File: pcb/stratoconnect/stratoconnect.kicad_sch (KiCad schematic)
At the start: 38 parts, among them J1 Conn_Coaxial, J2 Conn_02x03_Odd_Even, J3 Conn_01x05_Male, J4 Conn_01x02_Male, J5 Conn_01x03_Male, SW1 SW_SPST, SW2 SW_SPST, U1 RF4463f30, U2 ATmega328PB-A, U3 TPS61022RWU, Y1 CSTNE16M0V530000R0

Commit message: WIP
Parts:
- added R10, R11: 22k, Resistor_SMD:R_0603_1608Metric, symbol Device:R_Small_US
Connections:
- net RX_LED is gone; now on net LED_RX: R7.1
- net TX_LED is gone; now on net LED_TX: R6.1
- net +5V: now also R10.1, R11.1
- net LED_RX: no longer U2.2 (PD4)
- net LED_TX: no longer U2.1 (PD3)
- net SCL: now also R10.2
- net SDA: now also R11.2
- net TRIG: now also U2.1 (PD3)
- no-connect marks 9 -> 13
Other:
- moved on the sheet: J3

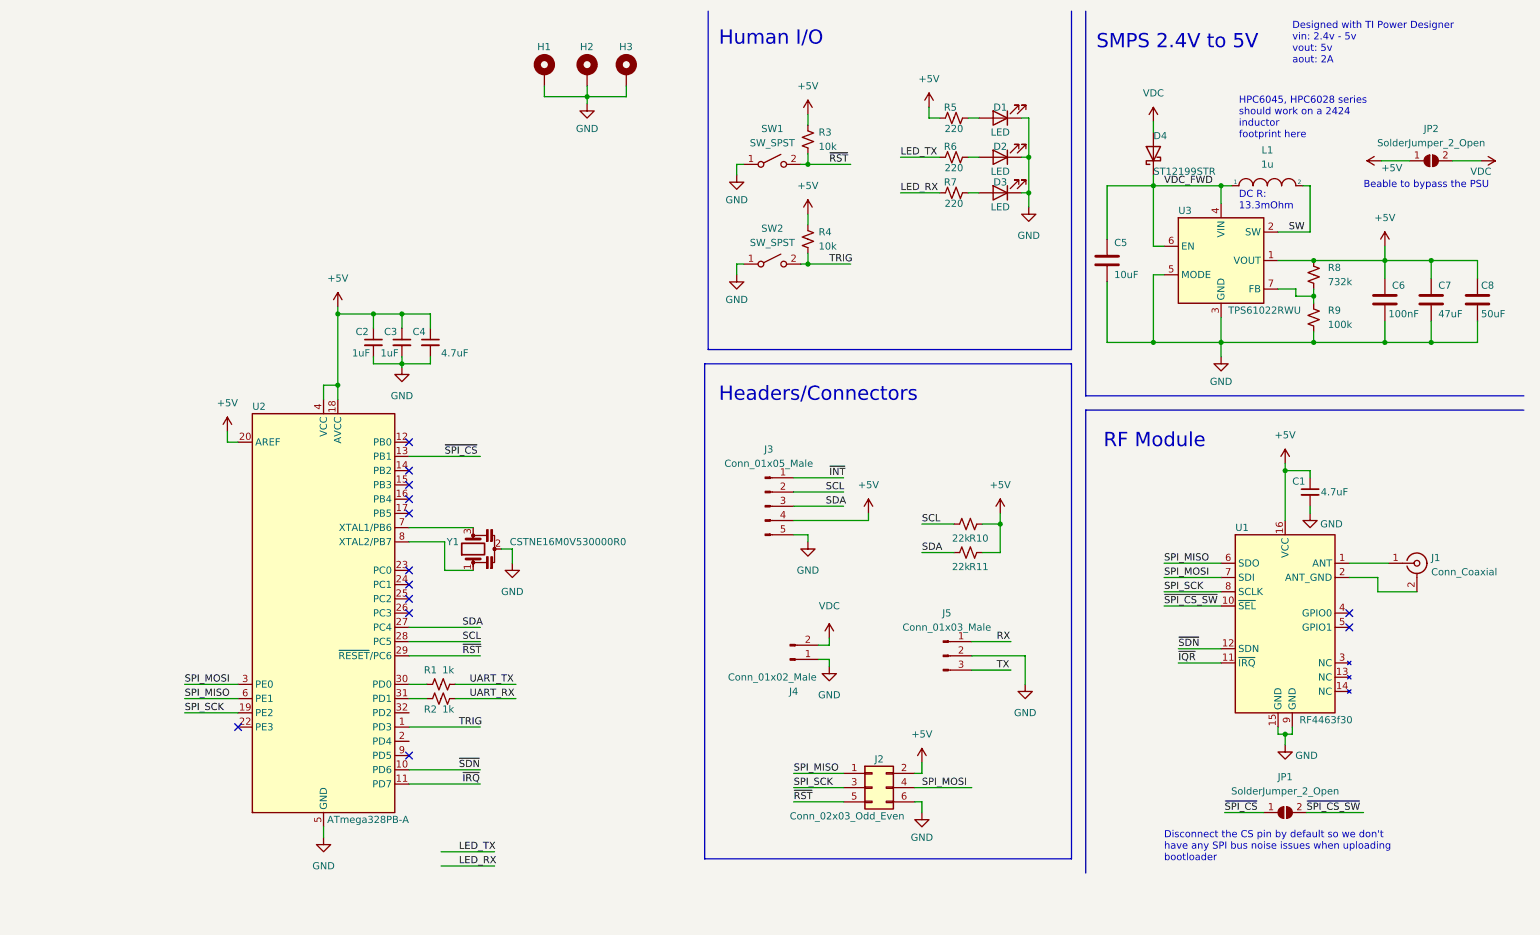
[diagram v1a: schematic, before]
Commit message: add some of the header labels we need. Finish routing everything but uart, the iscp header, and some other small stuff
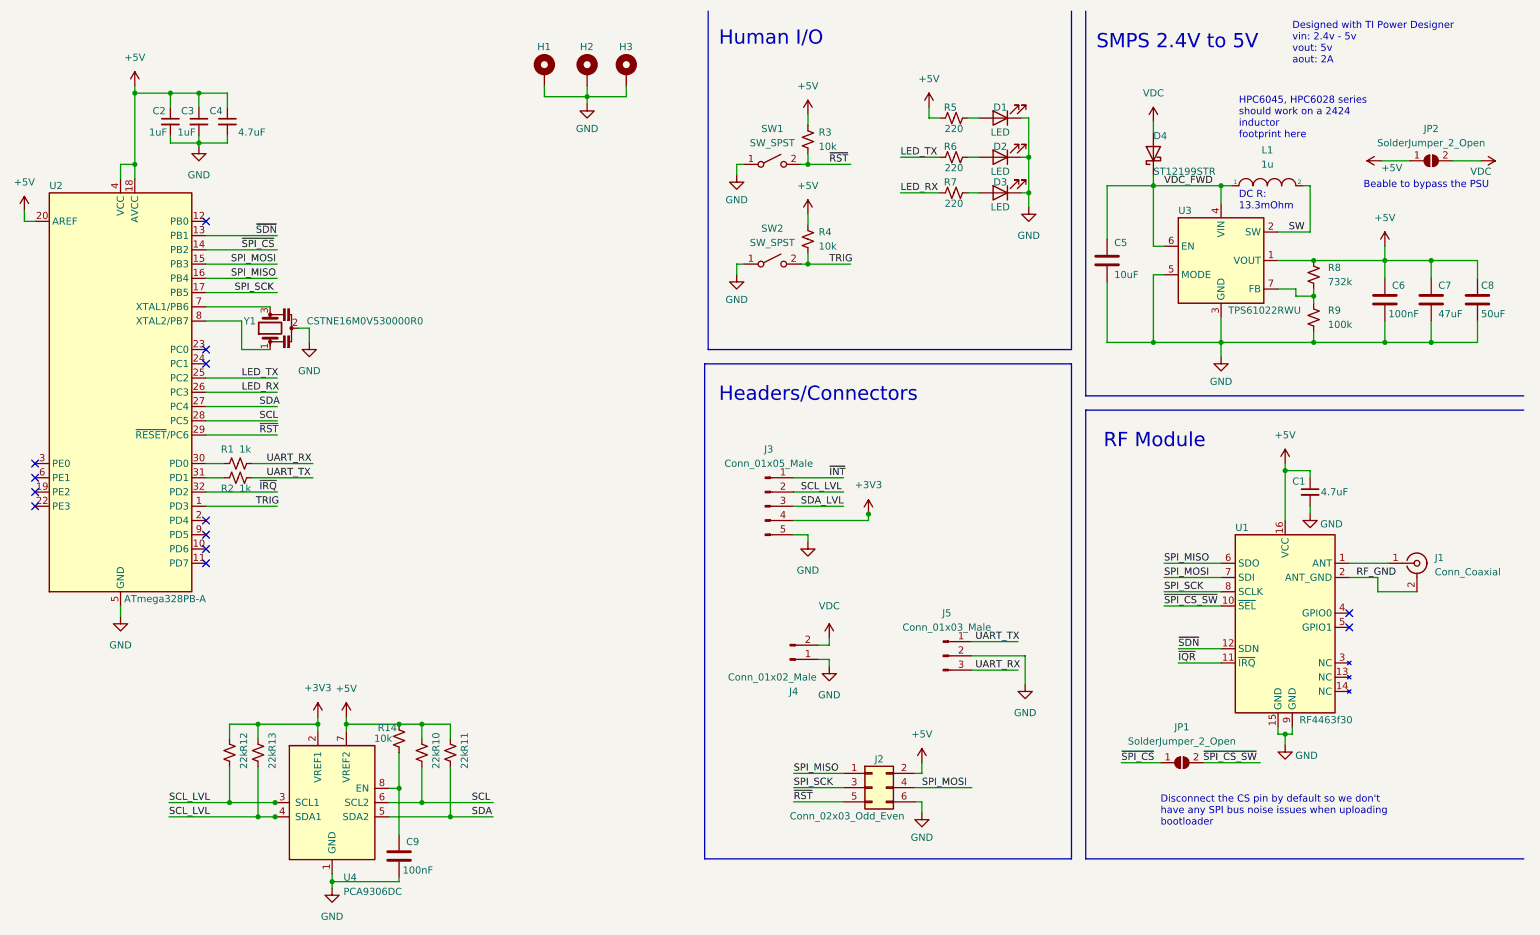
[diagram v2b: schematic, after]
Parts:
- added C9: 100nF, Capacitor_SMD:C_0603_1608Metric, symbol Device:C
- added R12, R13: 22k, Resistor_SMD:R_0603_1608Metric, symbol Device:R_Small_US
- added R14: 10k, Resistor_SMD:R_0603_1608Metric, symbol Device:R_Small_US
- added U4: PCA9306DC, Package_SO:VSSOP-8_2.3x2mm_P0.5mm, symbol Interface:PCA9306DC
- J1: footprint Connector_Coaxial:SMA_Molex_73251-2200_Horizontal -> Connector_Coaxial:SMA_Molex_73251-2120_EdgeMount_Horizontal
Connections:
- net RX is gone; now on net UART_TX: J5.1 (Pin_1)
- net TX is gone; now on net UART_RX: J5.3 (Pin_3)
- net +5V: now also R14.1, U4.7 (VREF2); no longer J3.4 (Pin_4)
- net GND: now also C9.2, U4.1 (GND)
- net LED_RX: now also U2.26 (PC3)
- net LED_TX: now also U2.25 (PC2)
- net SCL: now also U4.6 (SCL2); no longer J3.2 (Pin_2)
- net SDA: now also U4.5 (SDA2); no longer J3.3 (Pin_3)
- net SPI_MISO: now also U2.16 (PB4); no longer U2.6 (PE1)
- net SPI_MOSI: now also U2.15 (PB3); no longer U2.3 (PE0)
- net SPI_SCK: now also U2.17 (PB5); no longer U2.19 (PE2)
- net UART_RX: now also R1.2; no longer R2.2
- net UART_TX: now also R2.2; no longer R1.2
- net ~{IRQ}: now also U2.32 (PD2); no longer U2.11 (PD7)
- net ~{SDN}: now also U2.13 (PB1); no longer U2.10 (PD6)
- net ~{SPI_CS}: now also U2.14 (PB2); no longer U2.13 (PB1)
- net RF_GND: now reaches J1.2 (Ext), U1.2 (ANT_GND)
- new net: C9.1, R14.2, U4.8 (EN)
- new net +3V3: J3.4 (Pin_4), R12.1, R13.1, U4.2 (VREF1)
- new net SCL_LVL: J3.2 (Pin_2), R12.2, R13.2, U4.3 (SCL1), U4.4 (SDA1)
- new net SDA_LVL: J3.3 (Pin_3)
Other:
- moved on the sheet: C2, C3, C4, JP1, R1, R10, R11, R2, U2, Y1

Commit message: finish the design
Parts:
- removed JP1: SolderJumper_2_Open, Jumper:SolderJumper-2_P1.3mm_Open_RoundedPad1.0x1.5mm, symbol Jumper:SolderJumper_2_Open
- added C10: 100nF, Capacitor_SMD:C_0603_1608Metric, symbol Device:C_Small
- added JP1: SolderJumper_2_Bridged, symbol Jumper:SolderJumper_2_Bridged
- added JP3, JP4: SolderJumper_2_Open, Jumper:SolderJumper-2_P1.3mm_Open_RoundedPad1.0x1.5mm, symbol Jumper:SolderJumper_2_Open
- C8: value 50uF -> 47uF
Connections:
- net +5V: now also C10.1
- net GND: now also C10.2
- net SCL: now also JP3.2 (B)
- net SCL_LVL: now also JP3.1 (A); no longer R13.2, U4.4 (SDA1)
- net SDA: now also JP4.2 (B)
- net SDA_LVL: now also R13.2, U4.4 (SDA1), JP4.1 (A)
- net ~{INT}: now also U2.24 (PC1)
- net ~{SPI_CS_SW}: now also JP1.2 (B)
- net ~{SPI_CS}: now also JP1.1 (A)
- no-connect marks 13 -> 12
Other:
- note added: "Bypass the signal lever"
- note added: "I2C Level Shifting"
- moved on the sheet: C9, R10, R11, R12, R13, R14, U4

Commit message: add gerbers
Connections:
- net LED_RX: now also R6.1, U2.25 (PC2); no longer R7.1, U2.26 (PC3)
- net LED_TX: now also R7.1, U2.26 (PC3); no longer R6.1, U2.25 (PC2)

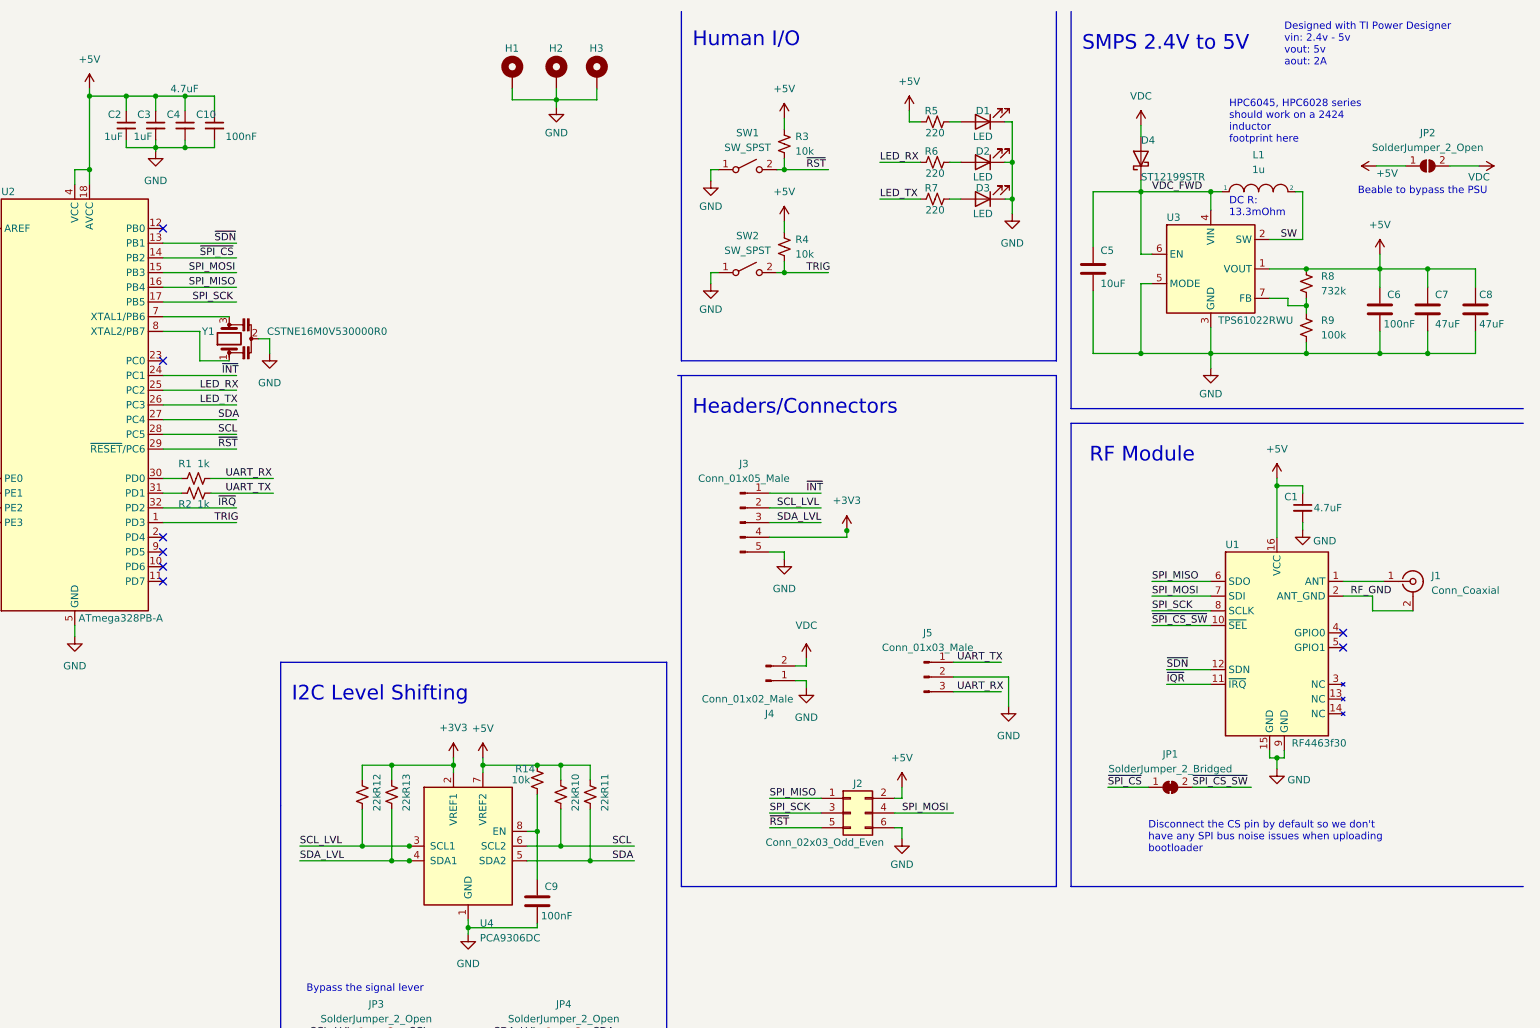
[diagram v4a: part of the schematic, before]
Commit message: add bom, readjust capactor annotations
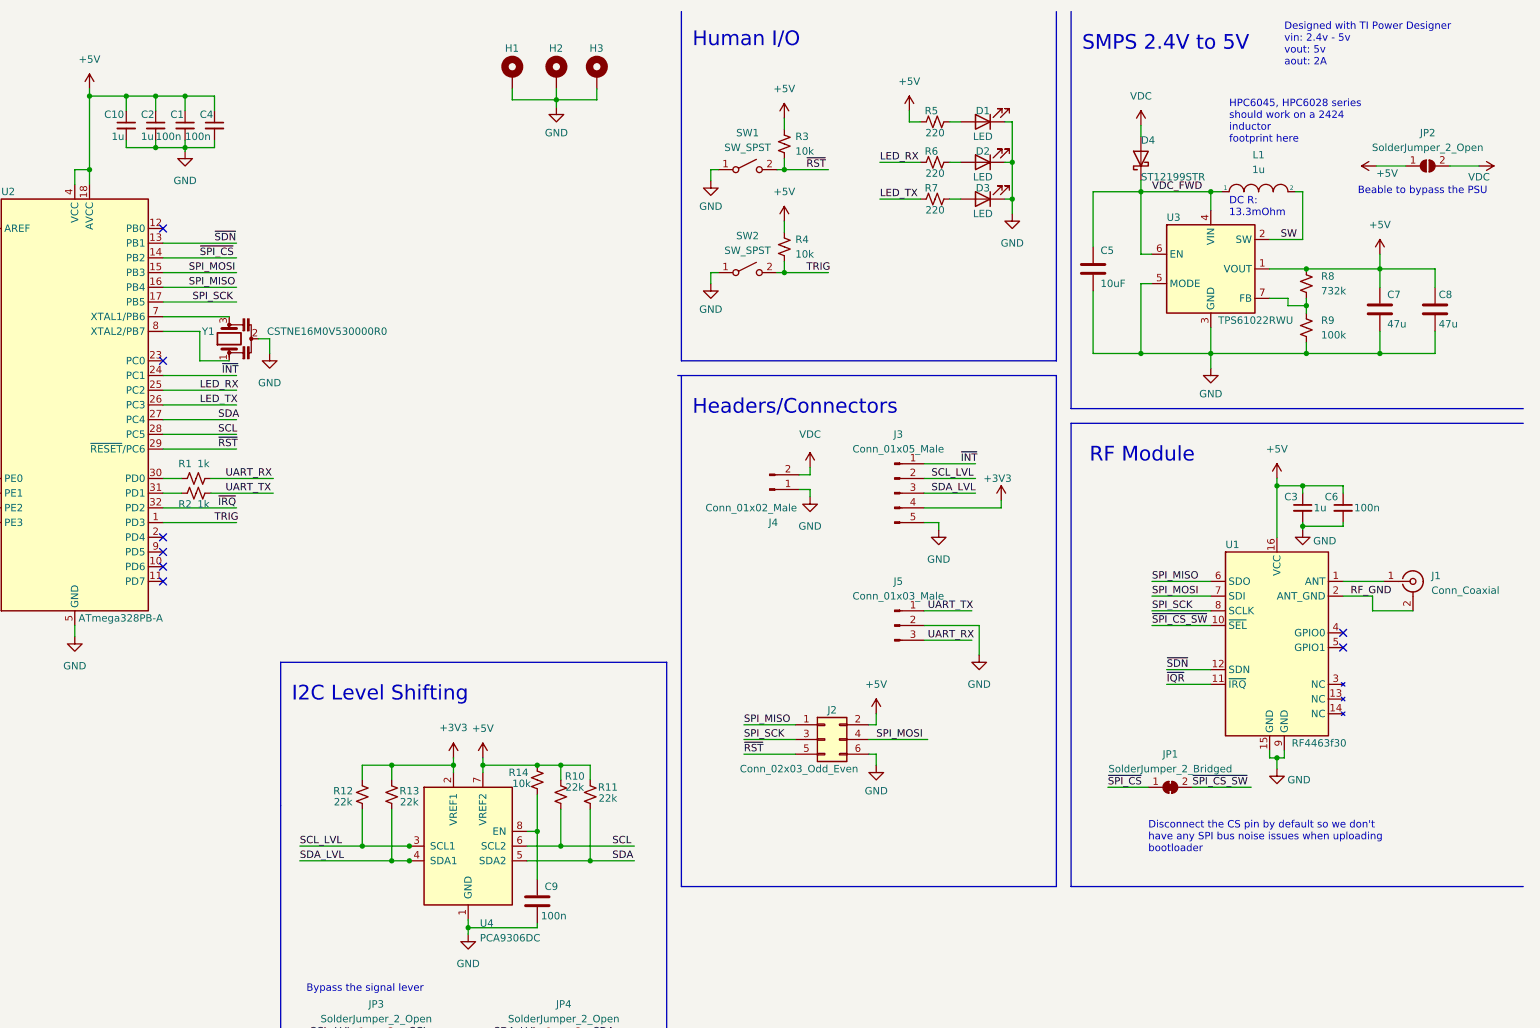
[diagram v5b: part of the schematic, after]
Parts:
- removed C6: 100nF, Capacitor_SMD:C_0603_1608Metric, symbol Device:C
- added C6: 100n, Capacitor_SMD:C_0603_1608Metric, symbol Device:C_Small
- C1: renamed from C3; value 1uF -> 100n
- C10: value 100nF -> 1u
- C2: value 1uF -> 1u
- C3: renamed from C1; value 4.7uF -> 1u
- C4: value 4.7uF -> 100n
- C7, C8: value 47uF -> 47u
- C9: value 100nF -> 100n
- JP1: footprint (none) -> Jumper:SolderJumper-2_P1.3mm_Bridged_RoundedPad1.0x1.5mm
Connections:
- net +5V: now also C6.1
- net GND: now also C6.2
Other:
- moved on the sheet: C1, C10, C2, C4, C7, C8, J2, J3, J4, J5
